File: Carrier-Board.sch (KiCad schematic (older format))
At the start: 45 parts, among them J1 CONN_3-6318491-6, J10 Conn_02x03_Odd_Even, J2 Conn_01x0, J3 Conn_02x26_Odd_Even, J4 SI-51009-F, J5 Conn_02x26_Odd_Even, J6 Conn_01x03_Male, J7 Conn_01x03_Male, J8 Conn_01x06_Male, J9 Conn_02x04_Odd_Even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

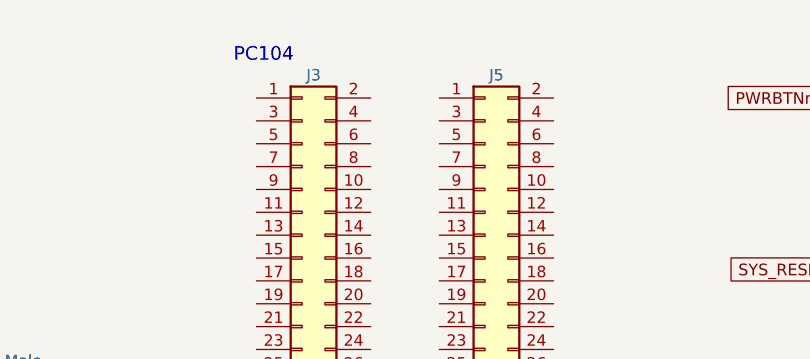
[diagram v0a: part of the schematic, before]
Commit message: Rename headers
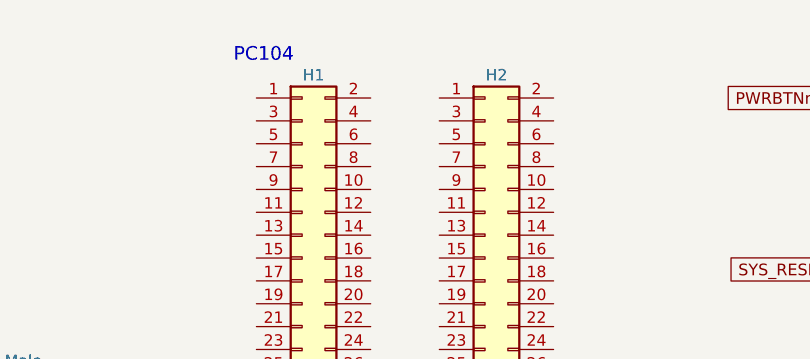
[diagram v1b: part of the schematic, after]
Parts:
- renumbered J3 to H1, J5 to H2
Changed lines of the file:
@@
 LIBS:Carrier-Board
 LIBS:SI-51009-F
-LIBS:Carrier-Board-cache
+LIBS:MCP6H04-E
+LIBS:BusSimulator
 EELAYER 25 0
 EELAYER END
@@
 $EndComp
 $Comp
-L Conn_02x26_Odd_Even J3
+L Conn_02x26_Odd_Even H1
 U 1 1 5A6C2591
 P 11900 2050
-F 0 "J3" H 11950 3350 50  0000 C CNN
+F 0 "H1" H 11950 3350 50  0000 C CNN
 F 1 "Conn_02x26_Odd_Even" H 11950 650 50  0000 C CNN
 F 2 "Carrier-Board:ESQ-126-XX-X-D" H 11900 2050 50  0001 C CNN
@@
 $EndComp
 $Comp
-L Conn_02x26_Odd_Even J5
+L Conn_02x26_Odd_Even H2
 U 1 1 5A6C25B0
 P 12700 2050
-F 0 "J5" H 12750 3350 50  0000 C CNN
+F 0 "H2" H 12750 3350 50  0000 C CNN
 F 1 "Conn_02x26_Odd_Even" H 12750 650 50  0000 C CNN
 F 2 "Carrier-Board:ESQ-126-XX-X-D" H 12700 2050 50  0001 C CNN
